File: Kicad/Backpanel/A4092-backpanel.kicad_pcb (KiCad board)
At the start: 2 copper layers, 24 x 72.2 mm, 2 parts, among them J1 Conn_02x25_Odd_Even, J2 5787170-5

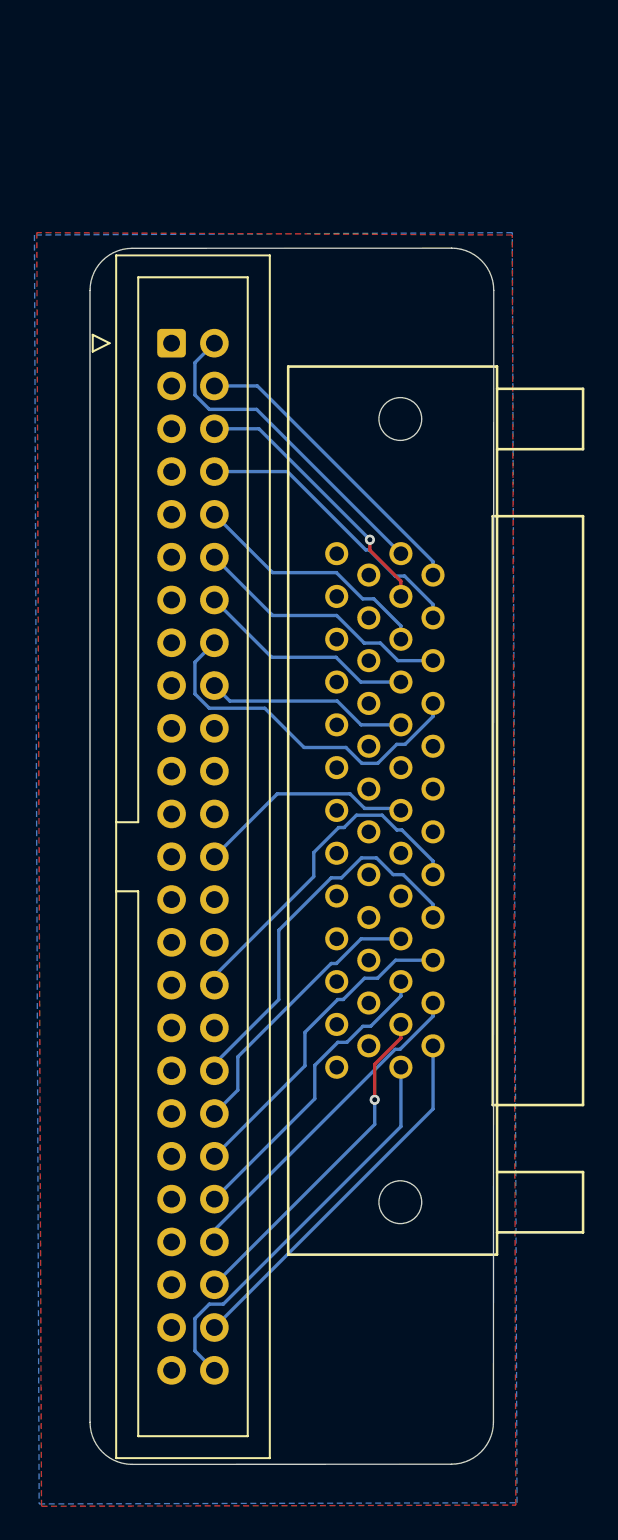
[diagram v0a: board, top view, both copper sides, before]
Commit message: Reduce backpanel size
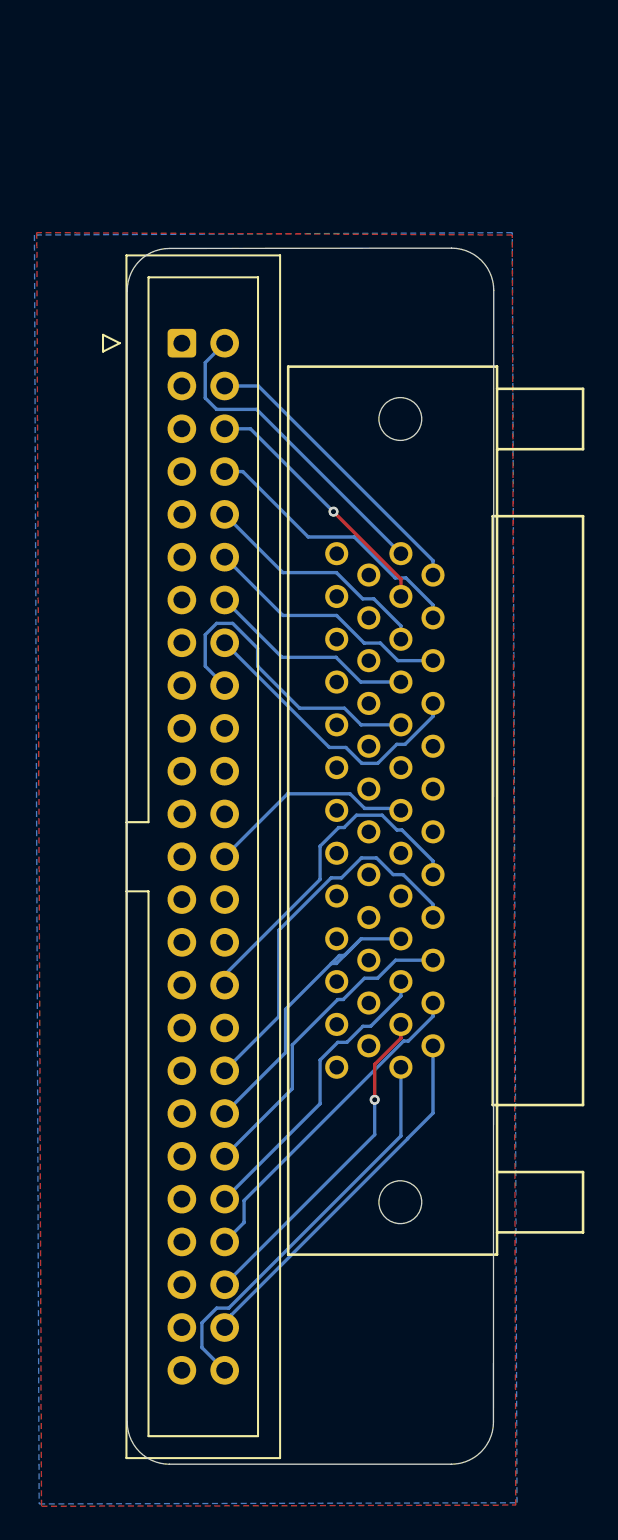
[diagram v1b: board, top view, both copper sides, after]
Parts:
- moved J1 0.61 mm to (156.5, 65.5)
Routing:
- net SCDATP: track 12.0 -> 18.5 mm
- net SCDAT7: track 21.3 -> 17.3 mm
- net SCTRL_ACK: track 16.5 -> 18.6 mm
- net SCDAT2: track 16.1 -> 15.2 mm
- net SCDAT3: track 17.0 -> 16.4 mm
- net SCSI_TERMPWR: track 13.0 -> 12.4 mm
- net SCDAT5: track 15.5 -> 14.9 mm
- net SCDAT6: track 13.1 -> 12.5 mm
- net SCDAT4: track 14.6 -> 14.0 mm
- net SCDAT1: track 18.1 -> 17.5 mm
- net SCDAT0: track 19.7 -> 19.2 mm
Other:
- board size 24 x 72.2 mm -> 21.8 x 72.2 mm

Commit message: Update Backpanel
- Fix part numbers and orientation
- Shift IDC50 connector up to get out of the way of the Zorro
  daughterboard and align better with the 4092 connector
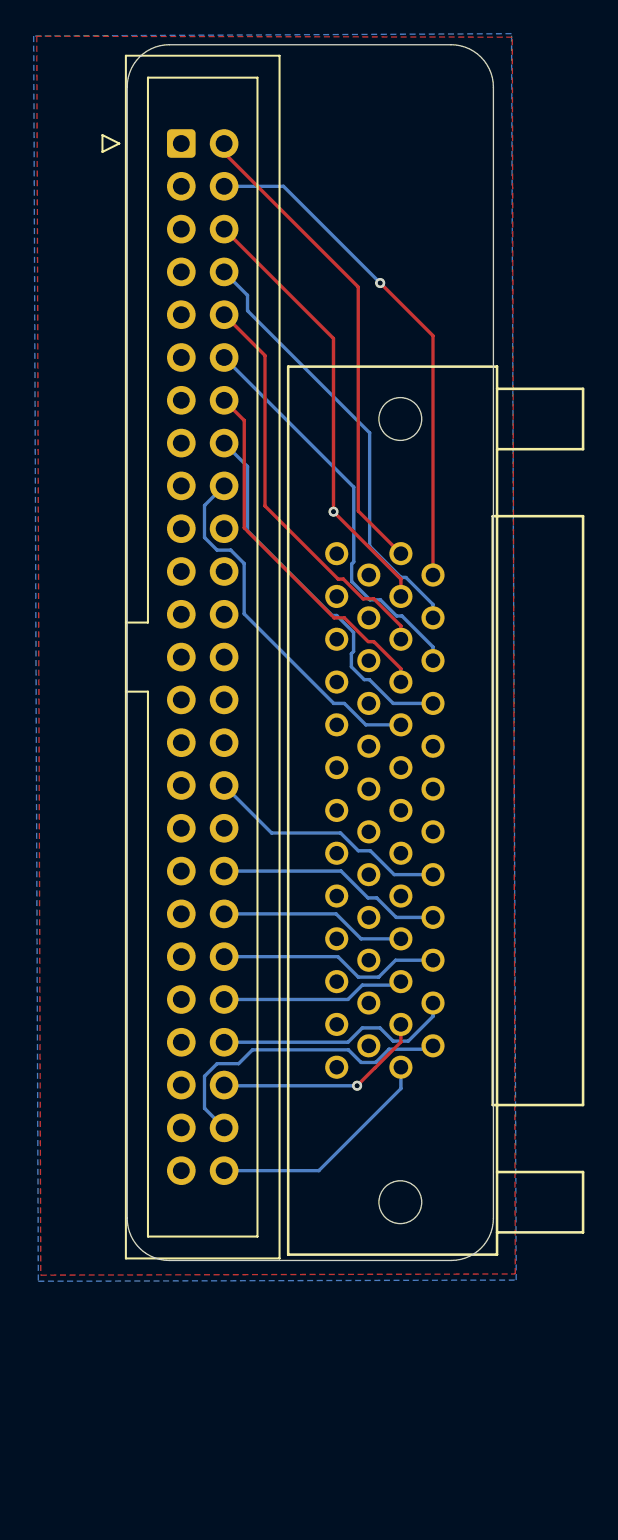
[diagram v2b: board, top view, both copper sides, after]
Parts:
- J2: value 5787170-5 -> TE Connectivity 5787395-5
- moved J1 11.9 mm to (156.5, 53.6)
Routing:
- net SCDAT1: track 17.5 -> 30.3 mm, vias 0 -> 1
- net SCSI_TERMPWR: track 12.4 -> 0.00 mm
- net SCDAT2: track 15.2 -> 26.1 mm
- net SCDAT4: track 14.0 -> 24.2 mm
- net SCTRL_IO: track 23.9 -> 13.8 mm
- net SCDAT0: track 19.2 -> 28.7 mm
- net SCDAT3: track 16.4 -> 25.8 mm
- net SCDAT6: track 12.5 -> 21.6 mm
- net SCTRL_BSY: track 22.5 -> 13.5 mm
- net SCDAT5: track 14.9 -> 23.8 mm
- net SCTRL_ACK: track 18.6 -> 11.1 mm
- net SCTRL_CD: track 19.8 -> 12.6 mm
- net SCTRL_MSG: track 17.8 -> 10.9 mm
- net SCTRL_ATN: track 20.0 -> 14.6 mm
- net SCTRL_RST: track 18.7 -> 13.3 mm
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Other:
- board size 21.8 x 72.2 mm -> 21.7 x 72.2 mm
